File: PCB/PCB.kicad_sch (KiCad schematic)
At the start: 43 parts, among them J1 USB_C_Receptacle_USB2.0_16P, J2 18650_PROTECTED, SW1 SW_Push, SW2 SW_Push, U1 HT-CT62, U2 SAM-M10Q, U3 ER_OLEDM0.91_1x-I2C, U4 TPS63001, U5 TPS22917DBV, U6 BQ24074RGT

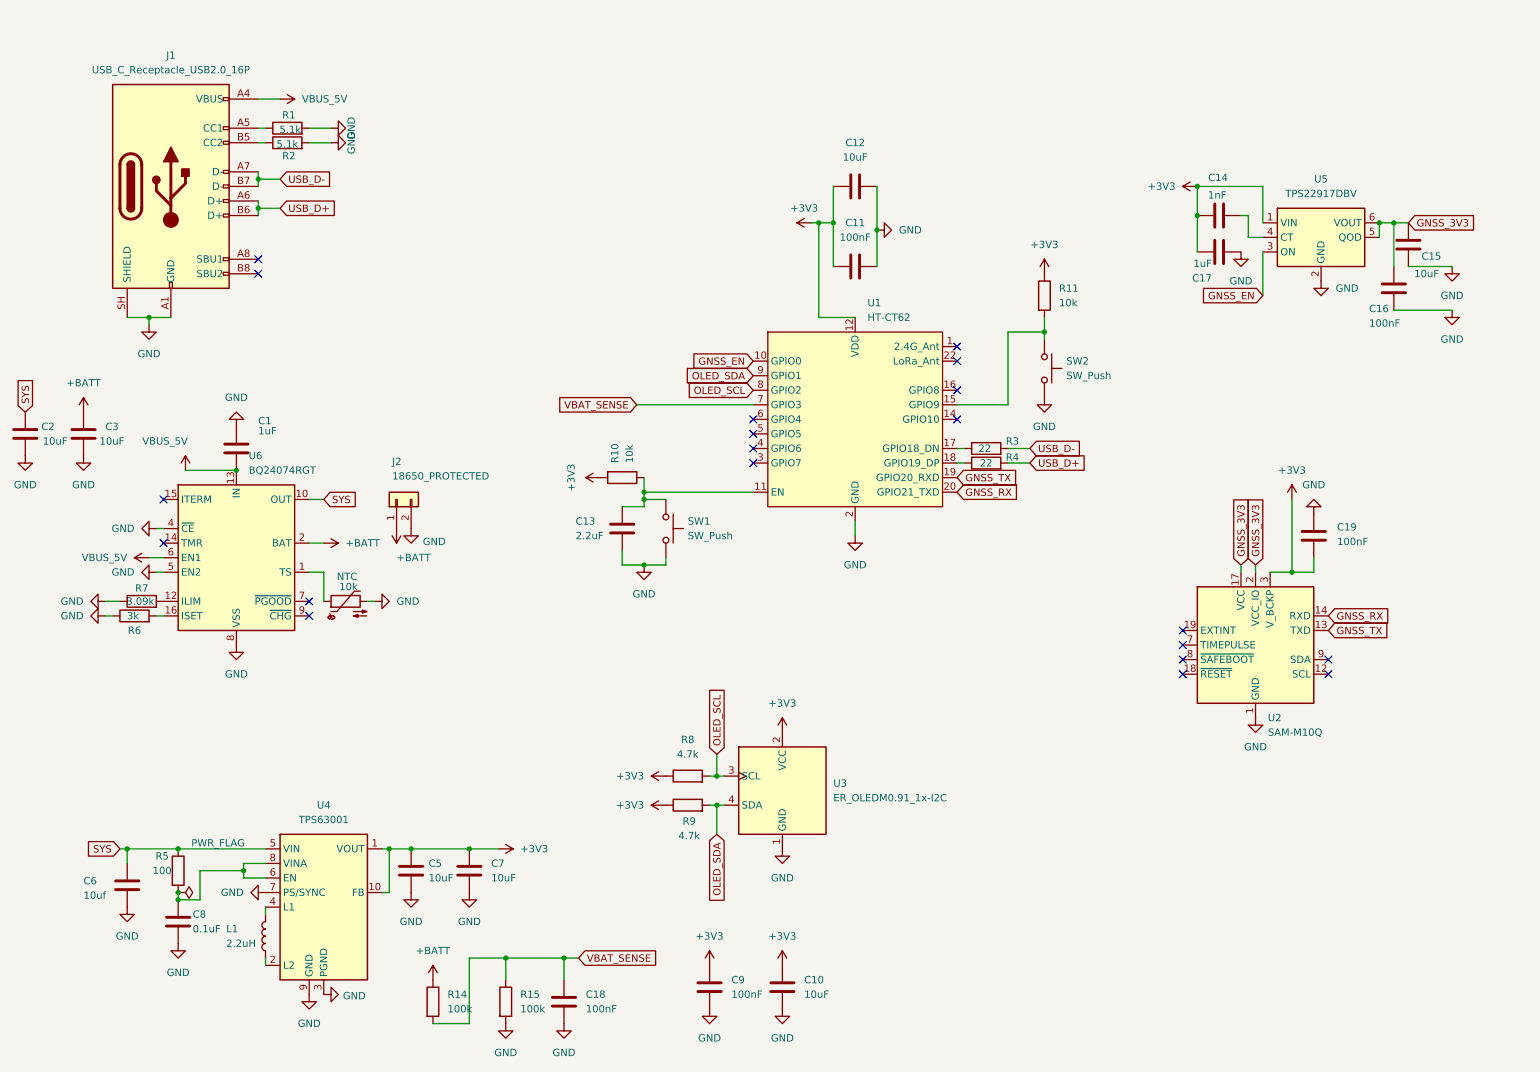
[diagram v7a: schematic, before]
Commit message: finishing schematic, assigning footprints
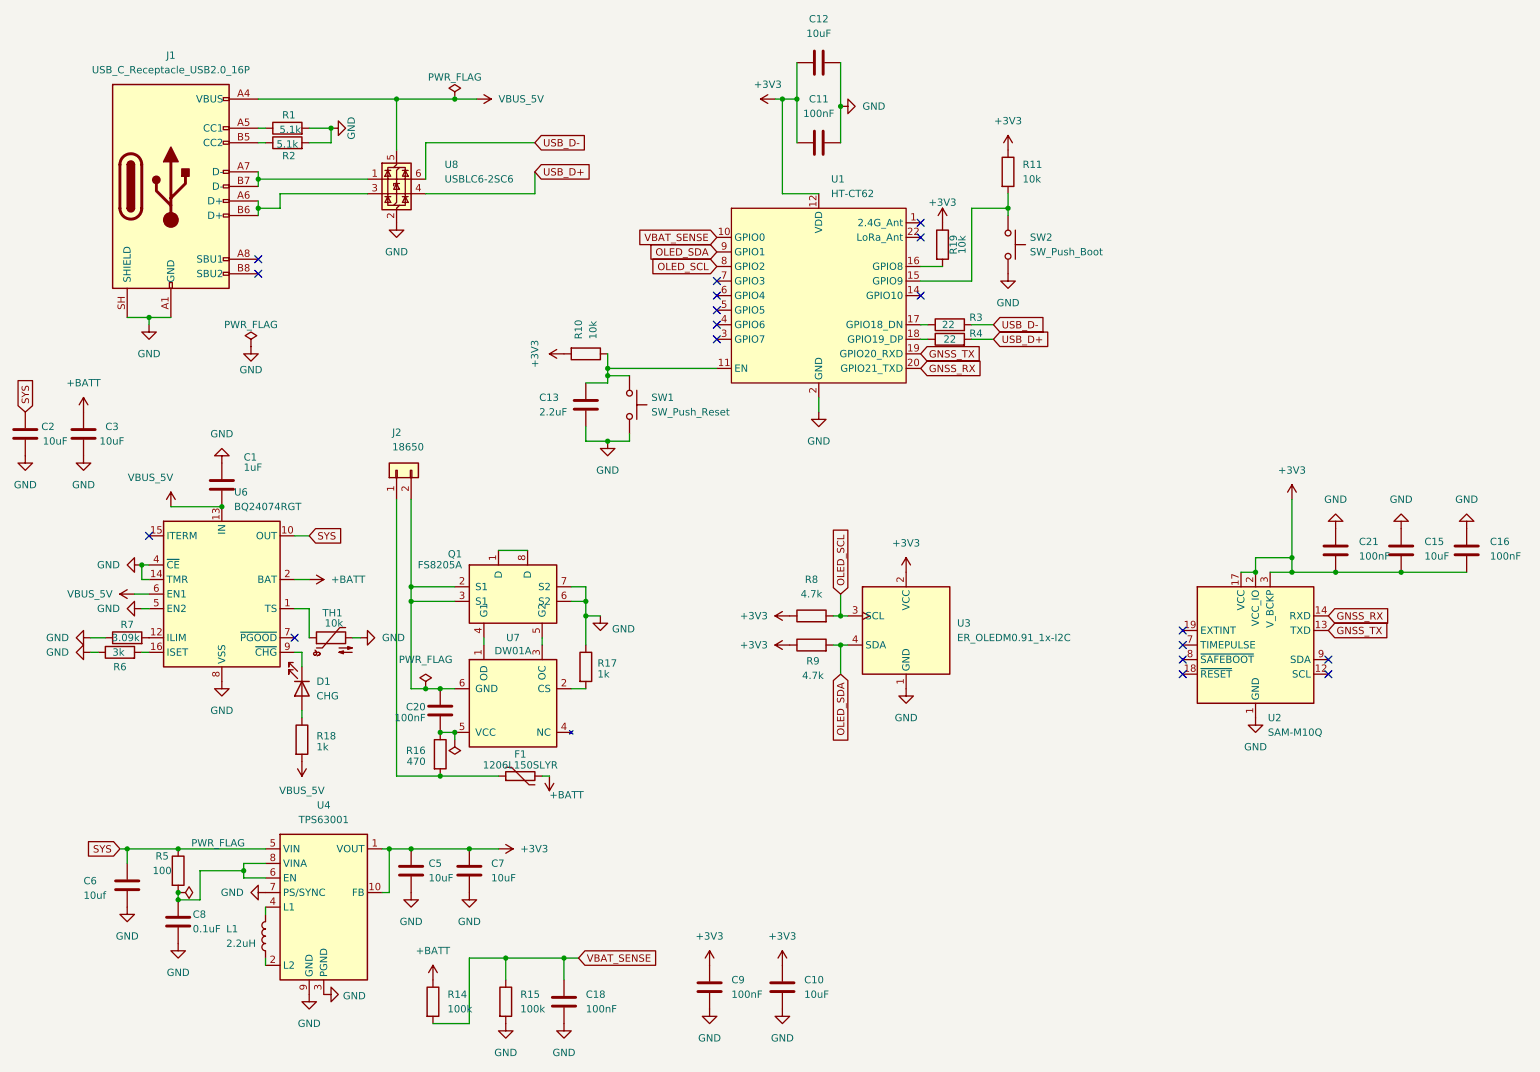
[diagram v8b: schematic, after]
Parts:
- removed C14: 1nF, symbol Device:C
- removed C17: 1uF, symbol Device:C
- removed C19: 100nF, symbol Device:C
- removed U5: TPS22917DBV, Package_TO_SOT_SMD:SOT-23-6, symbol Power_Management:TPS22917DBV
- added C20, C21: 100nF, Capacitor_SMD:C_0603_1608Metric, symbol Device:C
- added D1: CHG, LED_SMD:LED_0603_1608Metric, symbol Device:LED
- added F1: 1206L150SLYR, Fuse:Fuse_1206_3216Metric, symbol Node_Battery:Polyfuse
- added Q1: FS8205A, Package_SO:TSSOP-8_4.4x3mm_P0.65mm, symbol Node_Battery:FS8205A
- added R16: 470, Resistor_SMD:R_0603_1608Metric, symbol Device:R
- added R17, R18: 1k, Resistor_SMD:R_0603_1608Metric, symbol Device:R
- added R19: 10k, Resistor_SMD:R_0603_1608Metric, symbol Device:R
- added U7: DW01A, Package_TO_SOT_SMD:SOT-23-6, symbol Node_Battery:DW01A
- added U8: USBLC6-2SC6, Package_TO_SOT_SMD:SOT-23-6, symbol Power_Protection:USBLC6-2SC6
- C1, C11, C13, C16, C18, C8, C9: footprint (none) -> Capacitor_SMD:C_0603_1608Metric
- C10, C12, C15, C2, C3, C5, C6, C7: footprint (none) -> Capacitor_SMD:C_0805_2012Metric
- J1: footprint (none) -> Connector_USB:USB_C_Receptacle_HRO_TYPE-C-31-M-12
- J2: value 18650_PROTECTED -> 18650
- L1: footprint (none) -> Inductor_SMD:L_Taiyo-Yuden_NR-30xx
- R1, R10, R11, R14, R15, R2, R3, R4, R5, R6, R7, R8, R9: footprint (none) -> Resistor_SMD:R_0603_1608Metric
- SW1: value SW_Push -> SW_Push_Reset; footprint (none) -> Button_Switch_SMD:SW_SPST_PTS810
- SW2: value SW_Push -> SW_Push_Boot; footprint (none) -> Button_Switch_SMD:SW_SPST_PTS810
- TH1: renamed from NTC; footprint (none) -> Resistor_SMD:R_0603_1608Metric
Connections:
- net GNSS_EN is gone; now on net VBAT_SENSE: U1.10 (GPIO0)
- net +3V3: now also C15.1, C16.1, U2.17 (VCC), U2.2 (VCC_IO), C21.1, R19.1
- net +BATT: now also F1.2; no longer J2.1 (Pin_1)
- net GND: now also C15.2, C16.2, U6.14 (TMR), C21.2, Q1.6 (S2), Q1.7 (S2), R17.1, U8.2 (GND); no longer C15.1, C16.1, J2.2 (Pin_2)
- net USB_D+: now also U8.4 (I/O2); no longer J1.A6 (D+), J1.B6 (D+)
- net USB_D-: now also U8.6 (I/O1); no longer J1.A7 (D-), J1.B7 (D-)
- net VBAT_SENSE: no longer U1.7 (GPIO3)
- net VBUS_5V: now also R18.2, U8.5 (VBUS)
- net at U1.16 (GPIO8): now also R19.2
- net at U6.9 (~{CHG}): now also D1.1 (K)
- removed net GNSS_3V3: C15.2, C16.2, U2.17 (VCC), U2.2 (VCC_IO)
- new net: D1.2 (A), R18.1
- new net: F1.1, J2.1 (Pin_1), R16.2
- new net: C20.1, J2.2 (Pin_2), Q1.2 (S1), Q1.3 (S1), U7.6 (GND)
- new net: J1.A6 (D+), J1.B6 (D+), U8.3 (I/O2)
- new net: J1.A7 (D-), J1.B7 (D-), U8.1 (I/O1)
- new net: Q1.4 (G1), U7.1 (OD)
- new net: R17.2, U7.2 (CS)
- new net: Q1.5 (G2), U7.3 (OC)
- new net: C20.2, R16.1, U7.5 (VCC)
- new net: Q1.1 (D), Q1.8 (D)
- no-connect marks 20 -> 18
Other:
- moved on the sheet: C1, C11, C12, C13, J2, R10, R11, R3, R4, R6, R7, R8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
